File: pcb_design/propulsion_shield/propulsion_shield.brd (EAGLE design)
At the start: 100 x 80 mm, 62 parts

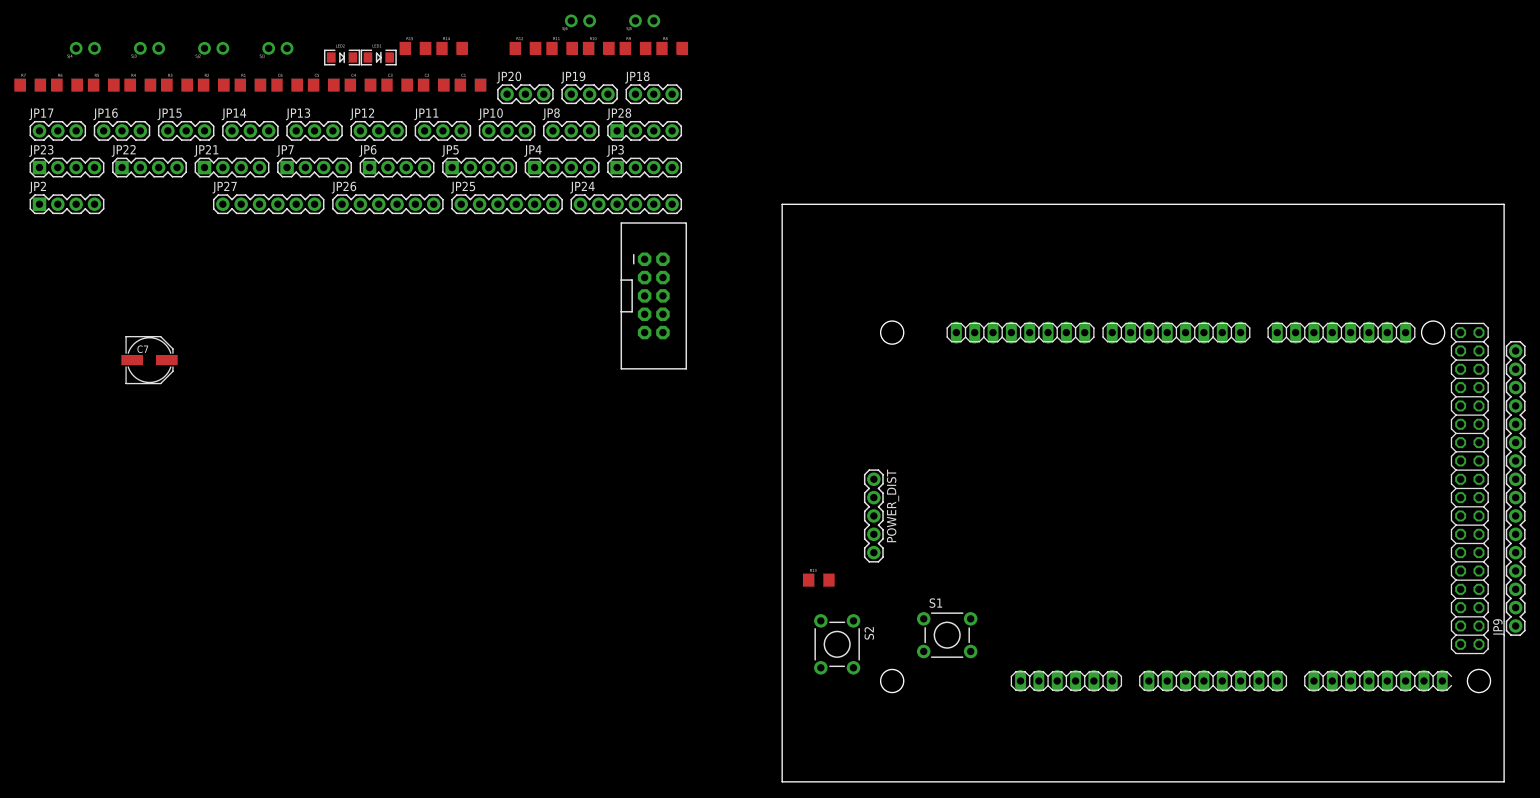
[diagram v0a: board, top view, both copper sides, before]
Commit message: [propulsion_shield] First draft of components placement + Bugfixes in schematics
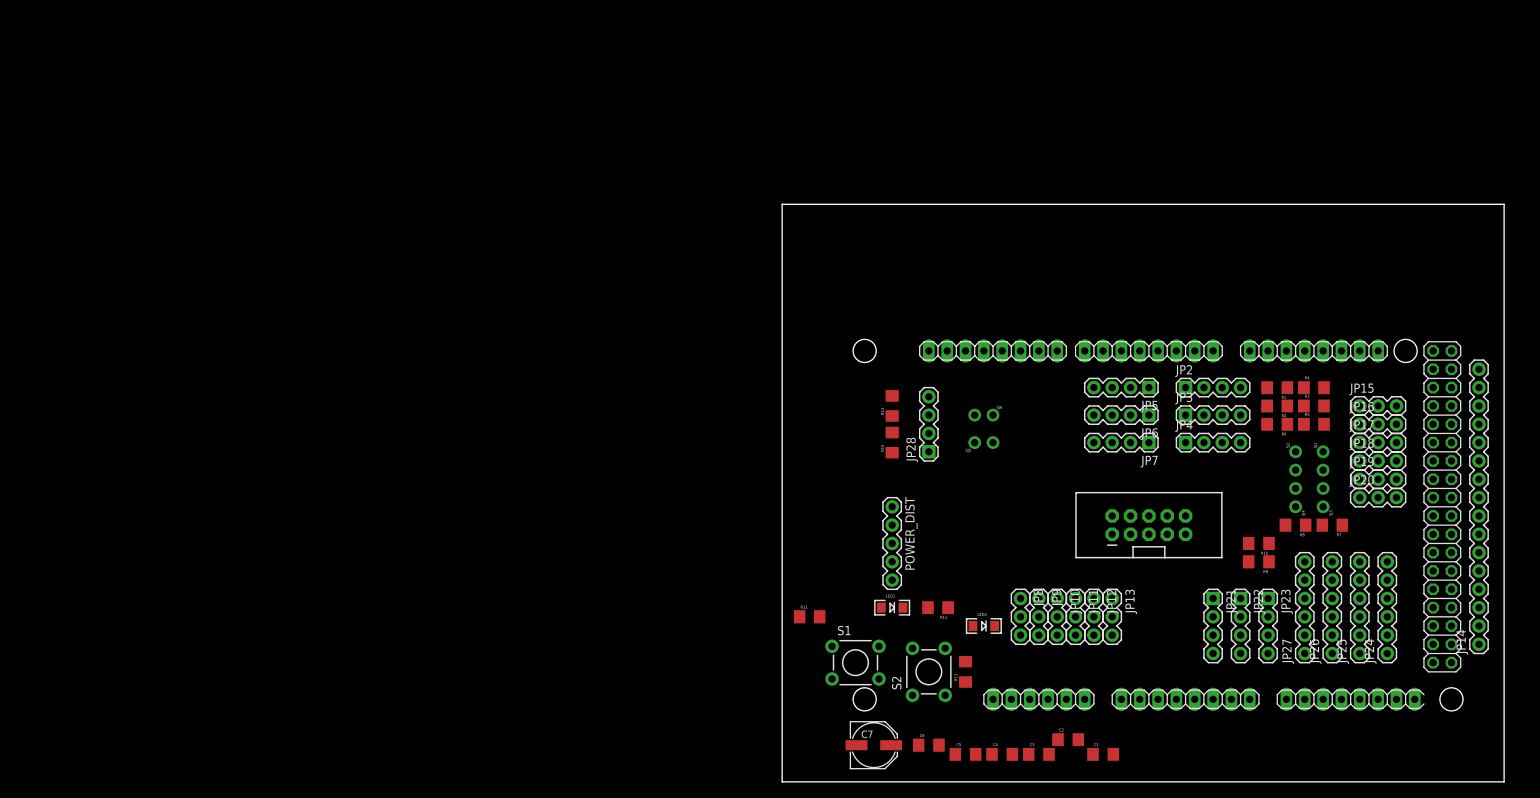
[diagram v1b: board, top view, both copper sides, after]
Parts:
- JP14: value (none) -> M16PTH; device SparkFun-Connectors:1X03 -> SparkFun-Connectors:1X16
- JP9: value M16PTH -> (none); device SparkFun-Connectors:1X16 -> SparkFun-Connectors:1X03
- moved R7 190.4 mm to (76.2, 35.6), turned to 180 degrees
- moved JP17 187.9 mm to (80.0, 47.0)
- moved JP14 186.8 mm to (96.5, 19.1), turned to 90 degrees
- moved JP23 180.3 mm to (67.3, 25.4), turned to 270 degrees
- moved SJ4 178.8 mm to (71.1, 39.4), turned to 90 degrees
- moved JP16 178.7 mm to (80.0, 49.5)
- moved R5 174.1 mm to (73.7, 49.5)
- moved R6 174.1 mm to (68.6, 49.5), turned to 180 degrees
- moved SJ3 174.1 mm to (74.9, 39.4), turned to 90 degrees
- moved JP15 169.4 mm to (80.0, 52.1)
- moved R4 167.9 mm to (73.7, 54.6)
- moved JP22 166.0 mm to (63.5, 25.4), turned to 270 degrees
- moved R3 163.6 mm to (73.7, 52.1)
- moved JP27 162.3 mm to (72.4, 17.8), turned to 90 degrees
- moved JP2 160.8 mm to (55.9, 54.6)
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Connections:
- net GND: now also JP14.1, JP9.2; no longer JP14.2, JP9.1
- net MOT1_1: now also JP5.2; no longer JP5.3
- net MOT1_2: now also JP5.3; no longer JP5.2
- net MOT2_1: now also JP6.2; no longer JP6.3
- net MOT2_2: now also JP6.3; no longer JP6.2
- net MOT3_1: now also JP7.2; no longer JP7.3
- net MOT3_2: now also JP7.3; no longer JP7.2
- net SCL_HW: no longer SJ2.2, SJ4.2
- net SDA_HW: now also SJ2.2, SJ4.2
- net SHARP_1: now also JP9.3; no longer JP10.3
- net SHARP_2: now also JP10.3; no longer JP11.3
- net SHARP_3: now also JP11.3; no longer JP12.3
- net SHARP_4: now also JP12.3; no longer JP13.3
- net SHARP_5: now also JP13.3; no longer JP14.3
- net UI_0: now also JP14.3; no longer JP9.3
- net UI_1: now also JP14.4; no longer JP9.4
- net UI_10: now also JP14.13; no longer JP9.13
- net UI_11: now also JP14.14; no longer JP9.14
- net UI_12: now also JP14.15; no longer JP9.15
- net UI_13: now also JP14.16; no longer JP9.16
- net UI_2: now also JP14.5; no longer JP9.5
- net UI_3: now also JP14.6; no longer JP9.6
- net UI_4: now also JP14.7; no longer JP9.7
- net UI_5: now also JP14.8; no longer JP9.8
- net UI_6: now also JP14.9; no longer JP9.9
- net UI_7: now also JP14.10; no longer JP9.10
- net UI_8: now also JP14.11; no longer JP9.11
- net UI_9: now also JP14.12; no longer JP9.12
- net VCC: now also JP14.2, JP9.1; no longer JP14.1, JP9.2

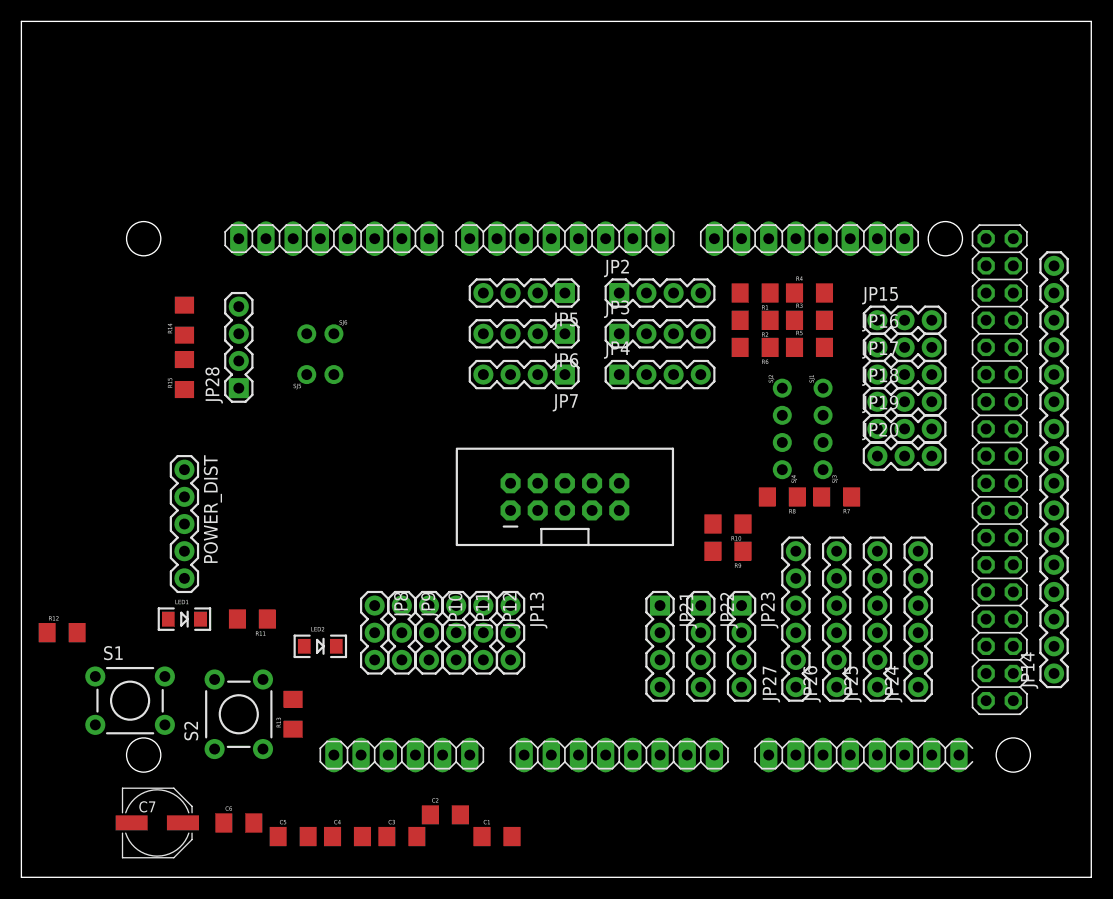
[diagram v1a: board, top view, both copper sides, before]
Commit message: [propulsion_shield] Full routing of the PCB
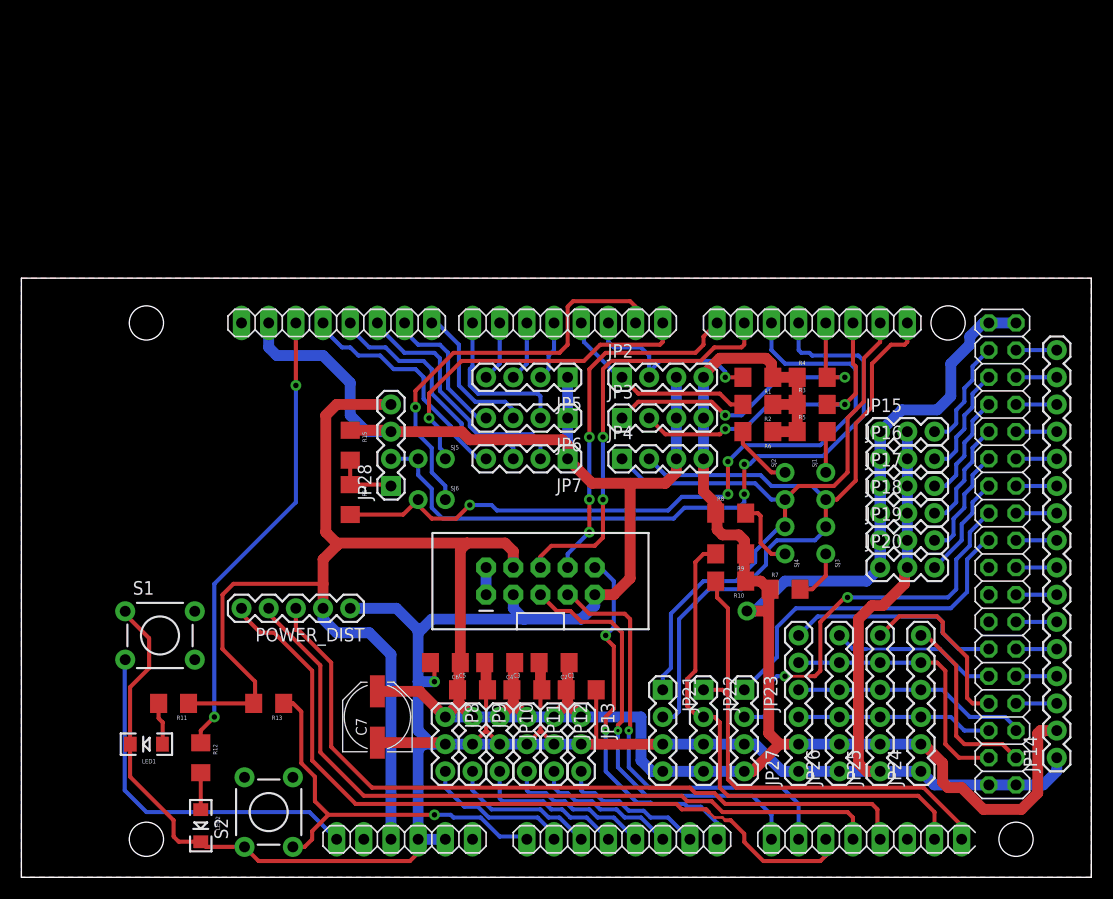
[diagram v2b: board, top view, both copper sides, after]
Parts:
- moved C6 24.4 mm to (39.6, 20.1), turned to 180 degrees
- moved C7 22.8 mm to (33.3, 15.0), turned to 90 degrees
- moved R14 22.8 mm to (30.7, 35.3), turned to 270 degrees
- moved C5 21.7 mm to (42.2, 17.5)
- moved C4 21.6 mm to (44.7, 20.1), turned to 180 degrees
- moved POWER_DIST 20.2 mm to (30.7, 25.1), turned to 180 degrees
- moved LED2 20.1 mm to (16.8, 4.83), turned to 270 degrees
- moved SJ6 18.7 mm to (38.4, 35.3)
- moved C3 18.0 mm to (47.2, 17.5)
- moved C2 17.5 mm to (49.8, 20.1), turned to 180 degrees
- moved R12 17.4 mm to (16.8, 11.2), turned to 270 degrees
- moved JP28 16.9 mm to (34.5, 36.6)
- moved R15 16.8 mm to (30.7, 40.4), turned to 270 degrees
- moved C1 15.8 mm to (52.3, 17.5)
- moved SJ5 13.1 mm to (38.4, 39.1), turned to 180 degrees
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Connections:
- net SCL_SW1: now also IC1.21; no longer IC1.22
- net SDA_SW1: now also IC1.22; no longer IC1.21
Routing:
- net VCC: track 0.00 -> 371.3 mm, vias 0 -> 1
- net GND: track 0.00 -> 323.7 mm, vias 0 -> 1
- net BAT_0: track 0.00 -> 71.8 mm
- net BAT_2: track 0.00 -> 70.8 mm
- net BT_TX: track 0.00 -> 70.2 mm, vias 0 -> 3
- net SCL_HW: track 0.00 -> 70.2 mm
- net BAT_1: track 0.00 -> 69.8 mm
- net BT_RX: track 0.00 -> 68.7 mm, vias 0 -> 2
- net SDA_HW: track 0.00 -> 63.5 mm
- net SCL_SW1: track 0.00 -> 49.3 mm
- net SDA_SW1: track 0.00 -> 46.4 mm
- net LED_IND: track 0.00 -> 42.9 mm, vias 0 -> 2
- net EXT_S2: track 0.00 -> 41.3 mm, vias 0 -> 1
- net EXT_S1: track 0.00 -> 40.3 mm, vias 0 -> 1
- net EXT_RX: track 0.00 -> 39.5 mm, vias 0 -> 2
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- added copper zone on layer 1, net GND
- added copper zone on layer 16, net GND
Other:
- board size 100 x 80 mm -> 100 x 56 mm
